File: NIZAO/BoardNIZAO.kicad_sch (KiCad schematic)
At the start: 17 parts, among them J5 PZ254R-12-14P, SW1 TS-1088-AR02016, U1 ADS1115IDGS, U2 ESP32-S3-WROOM-1, U3 RS485-PROTECT

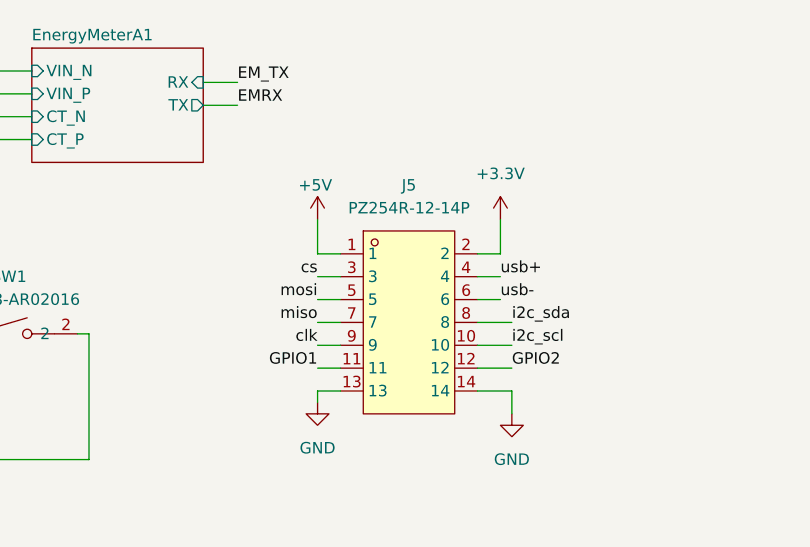
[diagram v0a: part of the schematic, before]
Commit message: Actualiza el mezzanine, eliminar assembly de prueba y actualizar essembly
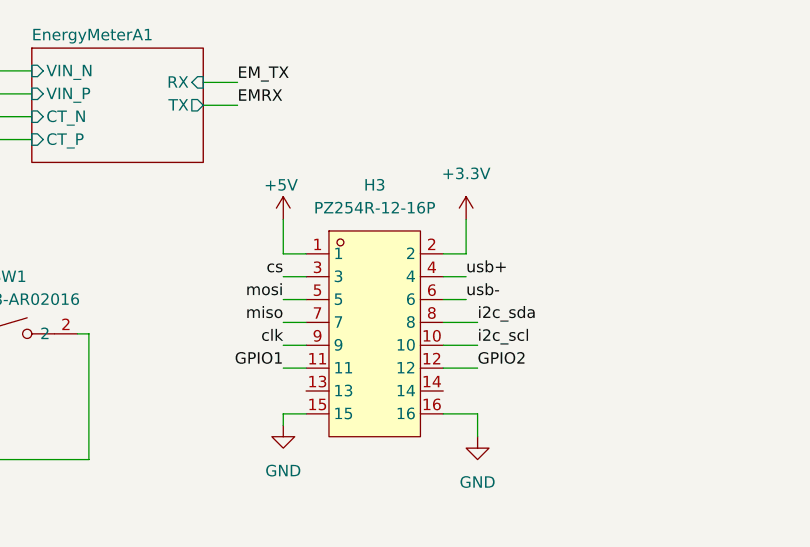
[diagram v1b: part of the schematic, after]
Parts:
- removed J5: PZ254R-12-14P, XFCN PZ254R-12-14P:HDR-TH_14P-P2.54-H-M-R2-C7-S2.54, symbol EasyEDA:PZ254R-12-14P
- added H3: PZ254R-12-16P, EasyEDA:HDR-TH_16P-P2.54-H-M-R2-C8-S2.54, symbol EasyEDA:PZ254R-12-16P
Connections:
- net +3.3V: now also H3.2
- net +5V: now also H3.1
- net GND: now also H3.15, H3.16
- net GPIO1: now also H3.11
- net GPIO2: now also H3.12
- net clk: now also H3.9
- net cs: now also H3.3
- net i2c_scl: now also H3.10
- net i2c_sda: now also H3.8
- net miso: now also H3.7
- net mosi: now also H3.5
- net usb+: now also H3.4
- net usb-: now also H3.6

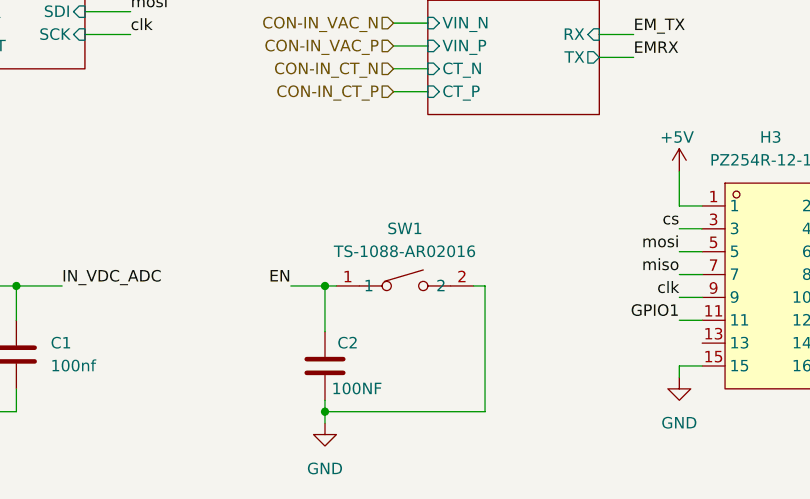
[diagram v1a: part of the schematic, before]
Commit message: Colocandos los 3d de los componetes en la placa NIZAO
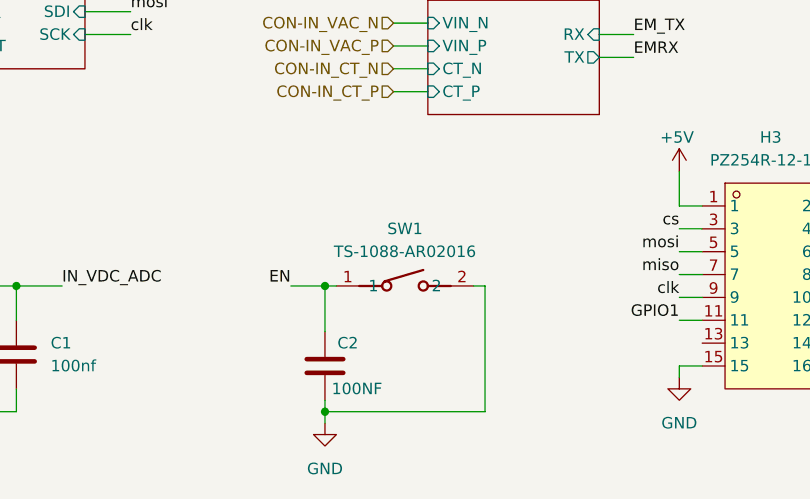
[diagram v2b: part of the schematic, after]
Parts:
- removed SW1: TS-1088-AR02016, XUNPU TS-1088-AR02016:SW-SMD_L3.9-W3.0-P4.45, symbol EasyEDA:TS-1088-AR02016
- added SW1: TS-1088-AR02016, JLCImport:TS-1088-AR02016, symbol JLCImport:TS-1088-AR02016
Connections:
- net EN: now also SW1.1
- net GND: now also SW1.2

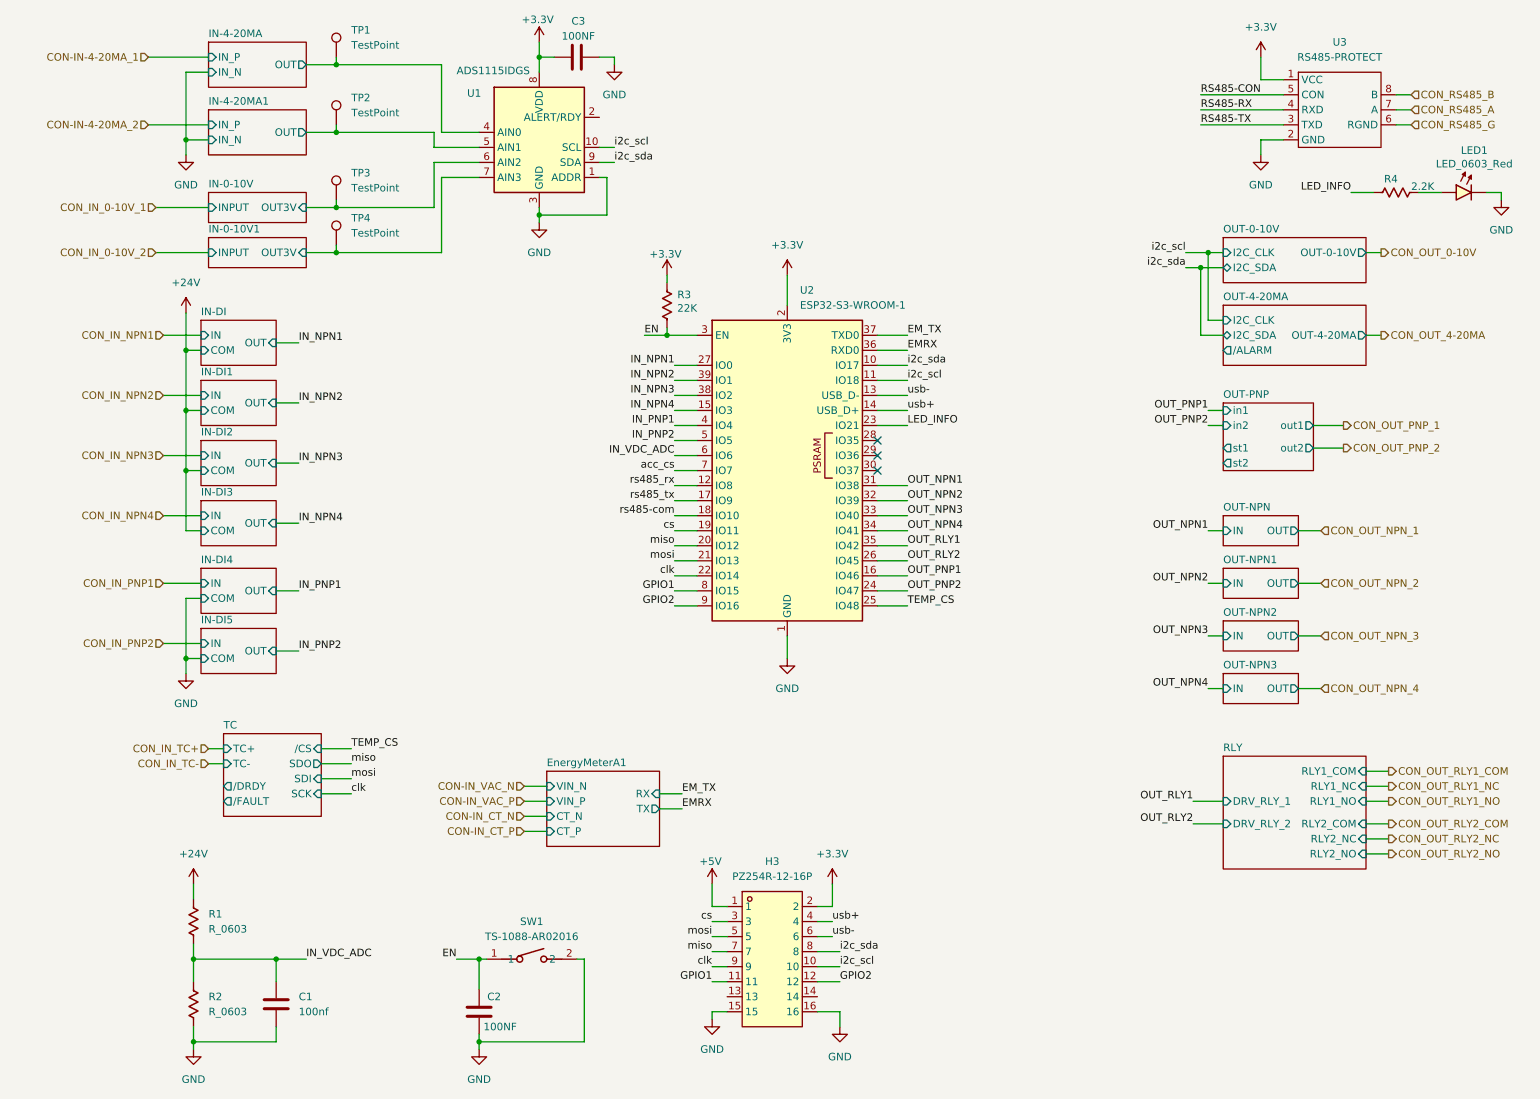
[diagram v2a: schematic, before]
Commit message: ACtualizandos las medidad del case de plastico y NIZAO
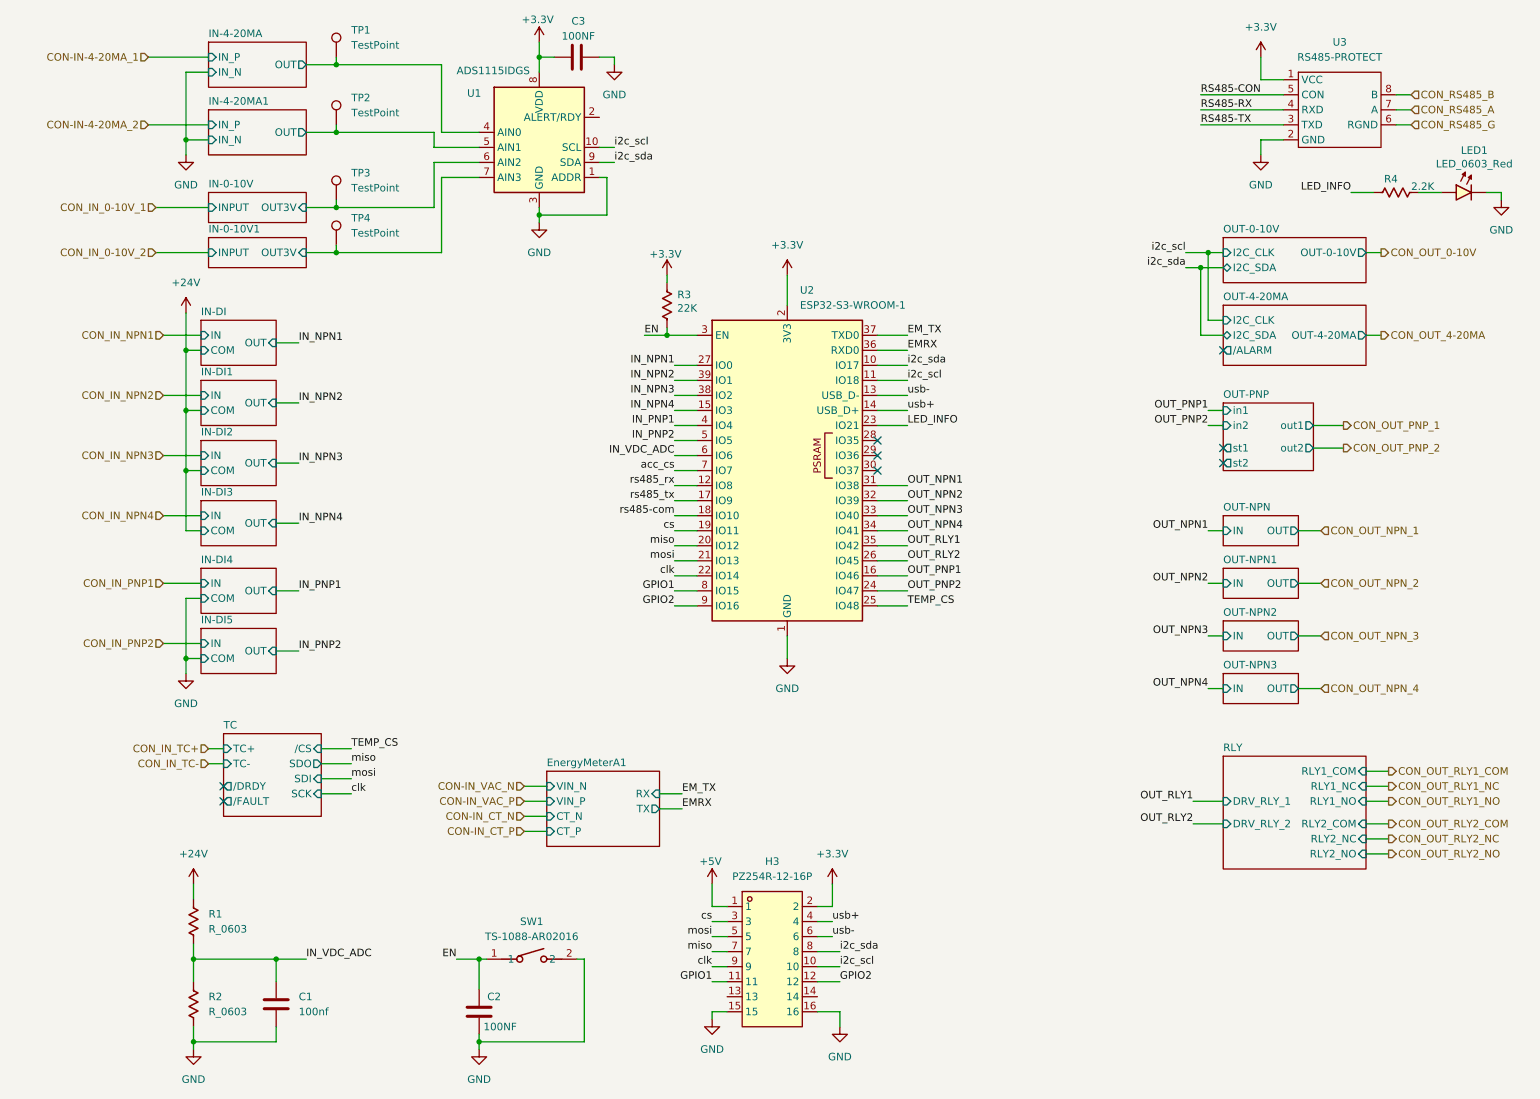
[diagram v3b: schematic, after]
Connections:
- no-connect marks 3 -> 8
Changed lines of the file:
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@@
+	)
+	(no_connect
+		(at 219.71 90.17)
 	)
 	(no_connect
@@
 	)
 	(no_connect
+		(at 50.8 144.78)
+	)
+	(no_connect
+		(at 219.71 71.12)
+	)
+	(no_connect
+		(at 50.8 147.32)
+	)
+	(no_connect
 		(at 161.29 86.36)
 	)
+	(no_connect
+		(at 219.71 87.63)
+	)
 	(wire
